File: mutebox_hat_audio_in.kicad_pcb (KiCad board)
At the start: 2 copper layers, 65 x 56 mm, 5 parts, among them J1 GPIO

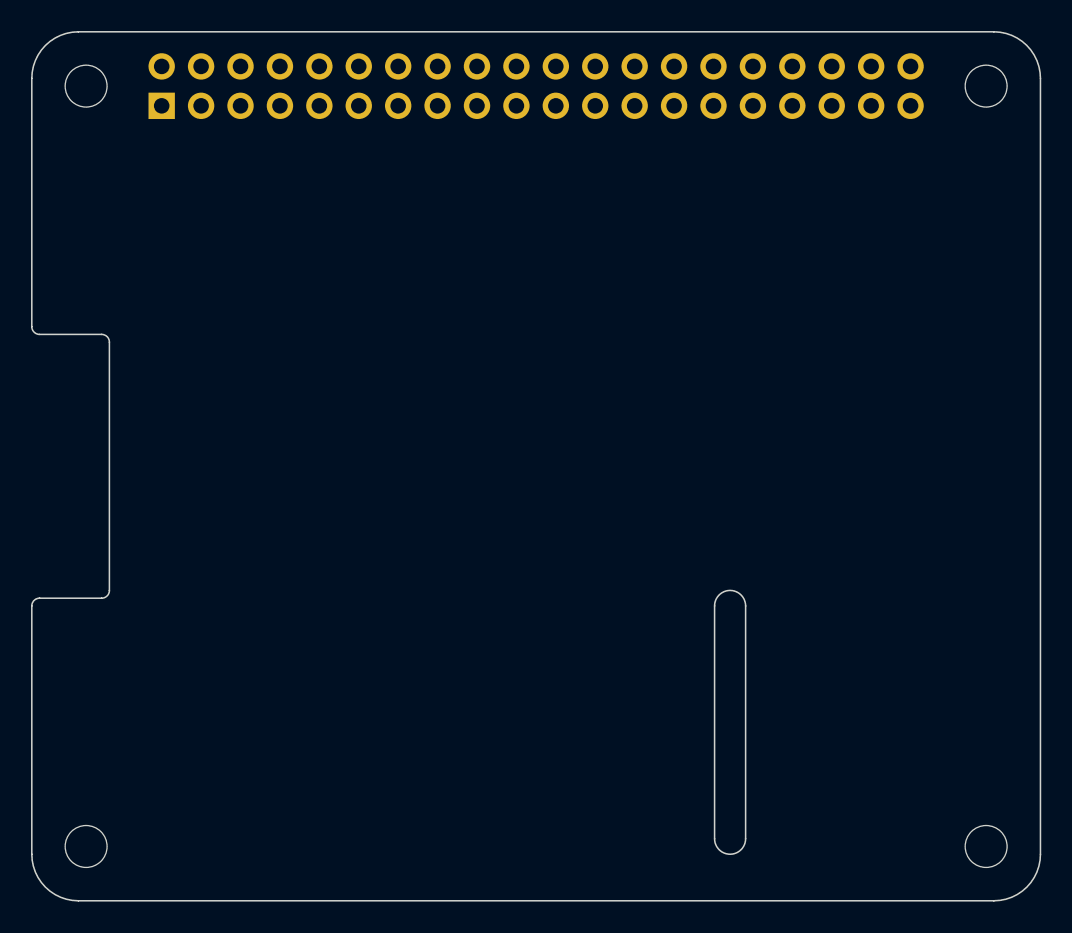
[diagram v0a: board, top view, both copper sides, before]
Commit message: switched to DIR9001PW for digital audio input
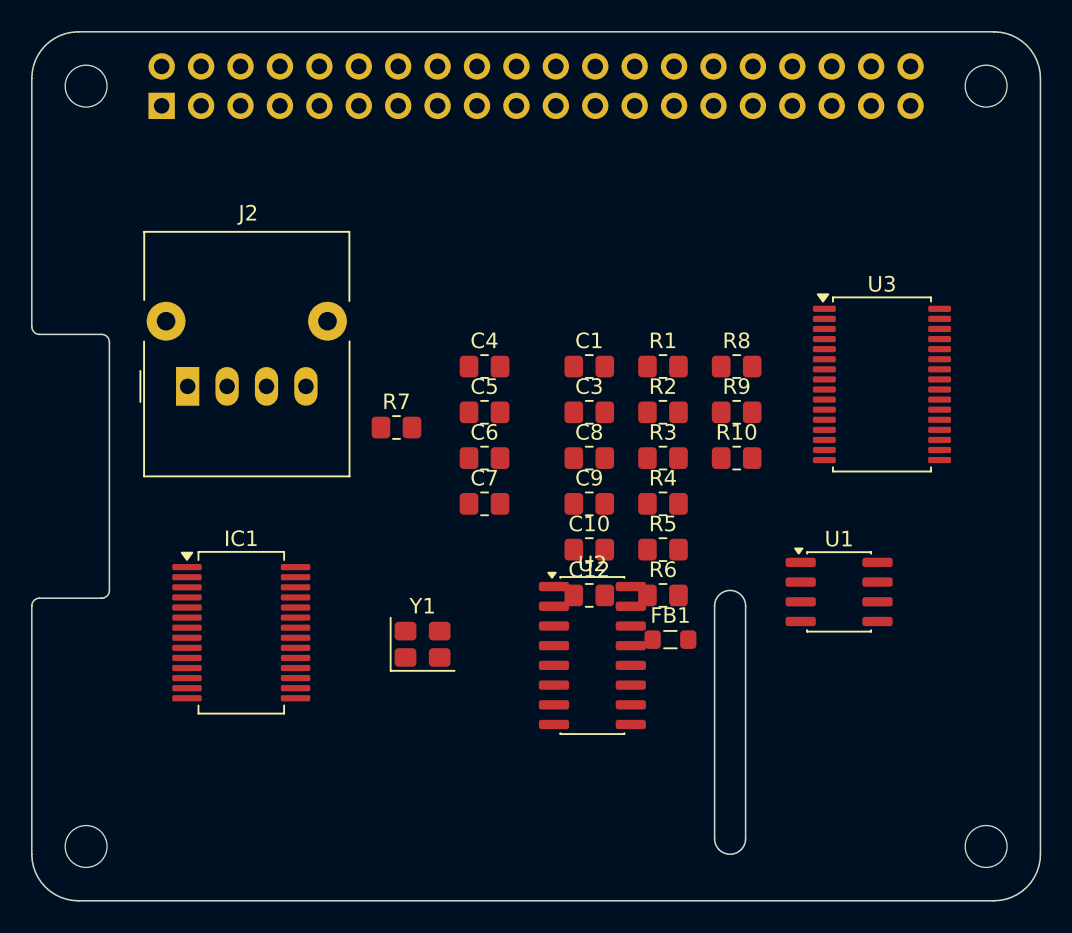
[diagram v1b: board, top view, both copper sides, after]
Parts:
- added C1: 100n, Resistor_SMD:R_0805_2012Metric_Pad1.20x1.40mm_HandSolder, F.Cu at (135.9, 65.6)
- added C10: 10uF, Resistor_SMD:R_0805_2012Metric_Pad1.20x1.40mm_HandSolder, F.Cu at (135.9, 77.4)
- added C12: 100nF, Resistor_SMD:R_0805_2012Metric_Pad1.20x1.40mm_HandSolder, F.Cu at (135.9, 80.3)
- added C3: 100NF, Resistor_SMD:R_0805_2012Metric_Pad1.20x1.40mm_HandSolder, F.Cu at (135.9, 68.5)
- added C4: C, Resistor_SMD:R_0805_2012Metric_Pad1.20x1.40mm_HandSolder, F.Cu at (129.2, 65.6)
- added C5: C, Resistor_SMD:R_0805_2012Metric_Pad1.20x1.40mm_HandSolder, F.Cu at (129.2, 68.5)
- added C6: 22pF, Resistor_SMD:R_0805_2012Metric_Pad1.20x1.40mm_HandSolder, F.Cu at (129.2, 71.5)
- added C7: 22pF, Resistor_SMD:R_0805_2012Metric_Pad1.20x1.40mm_HandSolder, F.Cu at (129.2, 74.4)
- added C8: 1uF (film preferred), Resistor_SMD:R_0805_2012Metric_Pad1.20x1.40mm_HandSolder, F.Cu at (135.9, 71.5)
- added C9: C, Resistor_SMD:R_0805_2012Metric_Pad1.20x1.40mm_HandSolder, F.Cu at (135.9, 74.4)
- added FB1: FerriteBead, Inductor_SMD:L_0805_2012Metric_Pad1.05x1.20mm_HandSolder, F.Cu at (141.2, 83.2)
- added IC1: WM8804GEDS_V, Package_SO:SSOP-28_5.3x10.2mm_P0.65mm, F.Cu at (113.5, 82.7)
- added J2: AFBR-2624Z, OptoDevice:Toshiba_TORX170_TORX173_TORX193_TORX194, F.Cu at (110.0, 66.8)
- added R1: 3.9k, Resistor_SMD:R_0805_2012Metric_Pad1.20x1.40mm_HandSolder, F.Cu at (140.7, 65.6)
- added R10: 4.7k, Resistor_SMD:R_0805_2012Metric_Pad1.20x1.40mm_HandSolder, F.Cu at (145.4, 71.5)
- added R2: 3.9k, Resistor_SMD:R_0805_2012Metric_Pad1.20x1.40mm_HandSolder, F.Cu at (140.7, 68.5)
- added R3: 10k, Resistor_SMD:R_0805_2012Metric_Pad1.20x1.40mm_HandSolder, F.Cu at (140.7, 71.5)
- added R4: 10k, Resistor_SMD:R_0805_2012Metric_Pad1.20x1.40mm_HandSolder, F.Cu at (140.7, 74.4)
- added R5: 10k, Resistor_SMD:R_0805_2012Metric_Pad1.20x1.40mm_HandSolder, F.Cu at (140.7, 77.4)
- added R6: 10k, Resistor_SMD:R_0805_2012Metric_Pad1.20x1.40mm_HandSolder, F.Cu at (140.7, 80.3)
- added R7: 10k, Resistor_SMD:R_0805_2012Metric_Pad1.20x1.40mm_HandSolder, F.Cu at (123.5, 69.5)
- added R8: 100k, Resistor_SMD:R_0805_2012Metric_Pad1.20x1.40mm_HandSolder, F.Cu at (145.4, 65.6)
- added R9: 4.7k, Resistor_SMD:R_0805_2012Metric_Pad1.20x1.40mm_HandSolder, F.Cu at (145.4, 68.5)
- added U1: CAT24C256, Package_SO:SOIC-8_3.9x4.9mm_P1.27mm, F.Cu at (152.0, 80.1)
- added U2: 74LVC157, Package_SO:SOIC-16_3.9x9.9mm_P1.27mm, F.Cu at (136.1, 84.2)
- added U3: PCM1862DBT, Package_SO:TSSOP-32_6.1x11mm_P0.65mm, F.Cu at (154.8, 66.7)
- added Y1: 12.288 MHz, Crystal:Crystal_SMD_3225-4Pin_3.2x2.5mm, F.Cu at (125.2, 83.5)
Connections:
- J1 pad 12: /GPIO18/PCM.CLK -> I2S_BCLK
- J1 pad 16: /GPIO23 -> SRC_SEL
- J1 pad 28: /ID_SCL -> ID_SC
- J1 pad 35: /GPIO19/PCM.FS -> I2S_SDIN
